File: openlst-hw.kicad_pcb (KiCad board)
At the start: 4 copper layers, 60 x 50 mm, 175 parts, among them J1 5VDC, J2 CC Prog/Debug, J3 UART0, J4 UART1, J5 Control Outputs, J6 ANT, U1 LM1117-3.3, U2 CC1110, U3 LT1086-3.6, U4 FOX924 27MHz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

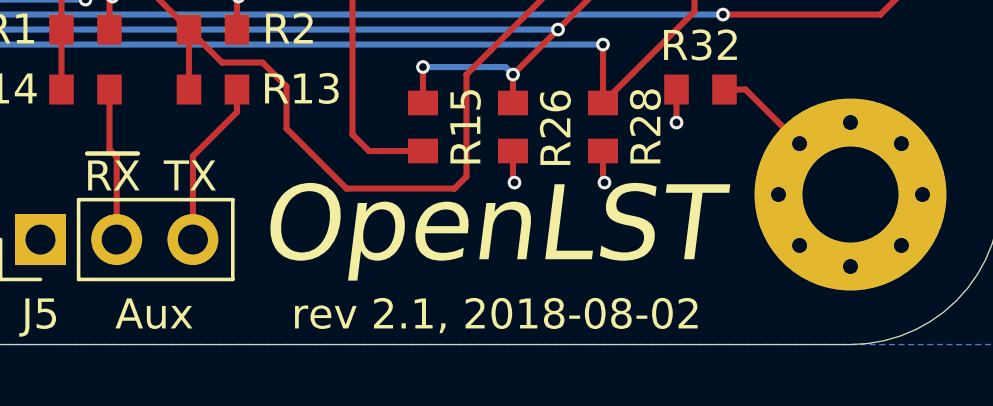
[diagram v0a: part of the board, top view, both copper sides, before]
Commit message: Modified silkscreen
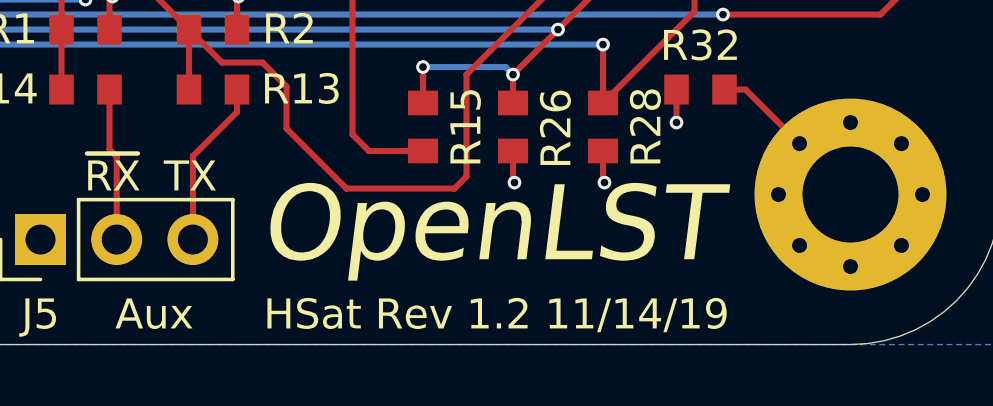
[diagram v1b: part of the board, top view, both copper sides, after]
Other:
- board text added: "HSat Rev 1.2 11/14/19"
- board text removed: "rev 2.1, 2018-08-02"
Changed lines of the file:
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@@
   (gr_arc (start 168.5 43.5) (end 168.5 38.5) (angle 90) (layer Edge.Cuts) (width 0.0254))
   (gr_arc (start 118.5 43.5) (end 113.5 43.5) (angle 90) (layer Edge.Cuts) (width 0.0254))
-  (gr_text "rev 2.1, 2018-08-02" (at 156.7 87.5) (layer F.SilkS)
+  (gr_text "HSat Rev 1.2 11/14/19" (at 156.7 87.5) (layer F.SilkS)
     (effects (font (size 1 1) (thickness 0.15)))
   )
